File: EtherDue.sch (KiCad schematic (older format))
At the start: 0 parts

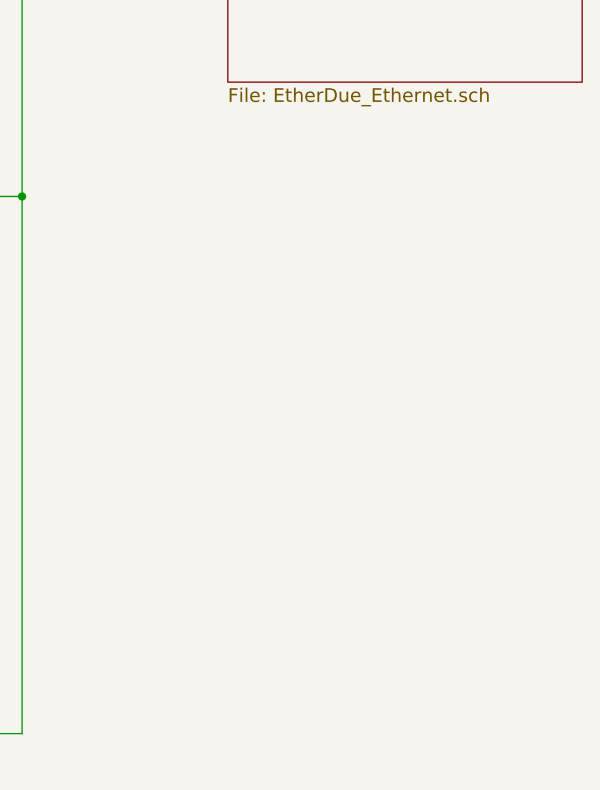
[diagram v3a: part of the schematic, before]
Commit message: Add 24AA025E48 EEPROM w/ unique MAC address
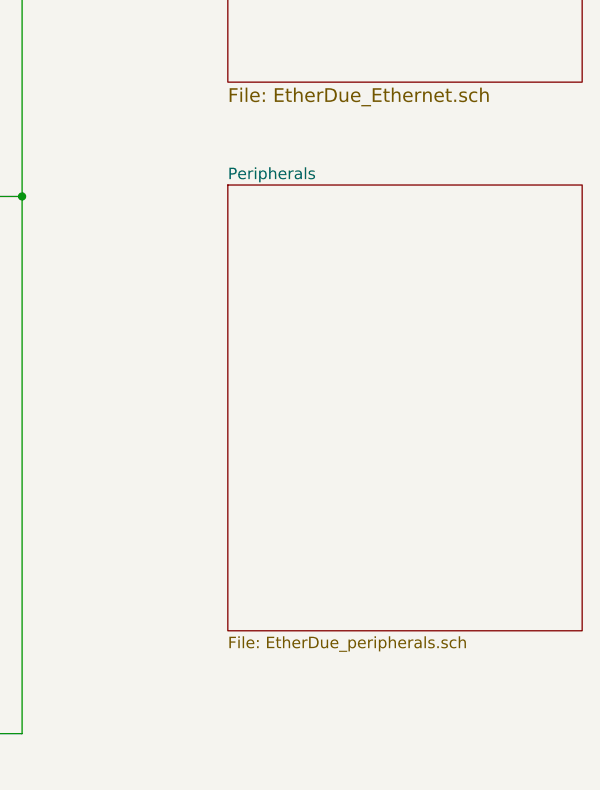
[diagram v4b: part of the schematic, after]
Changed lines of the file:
@@
-EESchema Schematic File Version 2  date Fri 28 Jun 2013 16:34:50 EST
+EESchema Schematic File Version 2  date Thu 04 Jul 2013 10:55:52 EST
 LIBS:freetronics_kicad_sch_lib
 LIBS:power
@@
 $Descr A4 11693 8268
 encoding utf-8
-Sheet 1 6
+Sheet 1 7
 Title ""
-Date "27 jun 2013"
+Date "4 jul 2013"
 Rev ""
 Comp ""
@@
 F2 "/MASTER-RESET" I L 7450 1300 60
 $EndSheet
+$Sheet
+S 7450 3600 1550 1950
+U 51D4D3EB
+F0 "Peripherals" 50
+F1 "EtherDue_peripherals.sch" 50
+$EndSheet
 $EndSCHEMATC

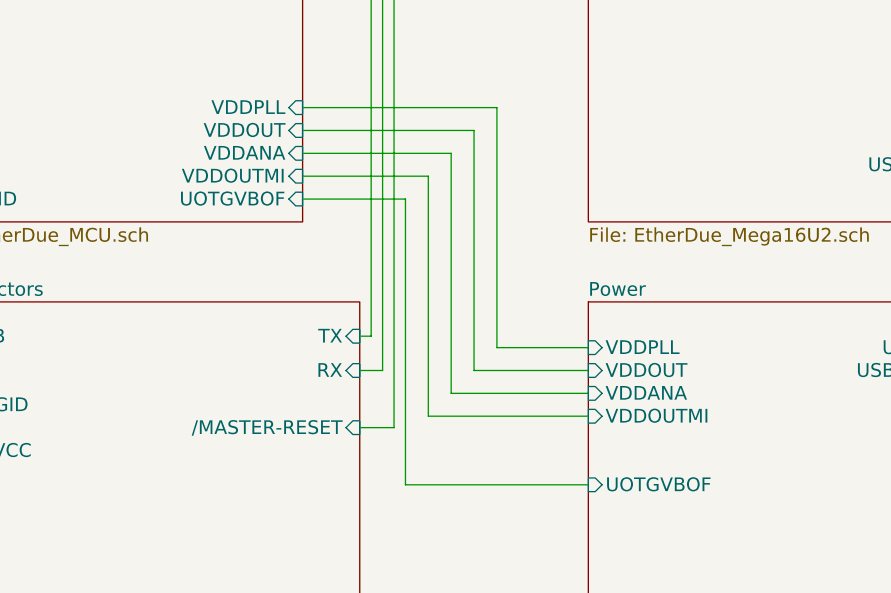
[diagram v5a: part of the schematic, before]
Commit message: Big power fixes: Fix major problem with VDDOUT/1.8V net, rearrange decoupling capacitors
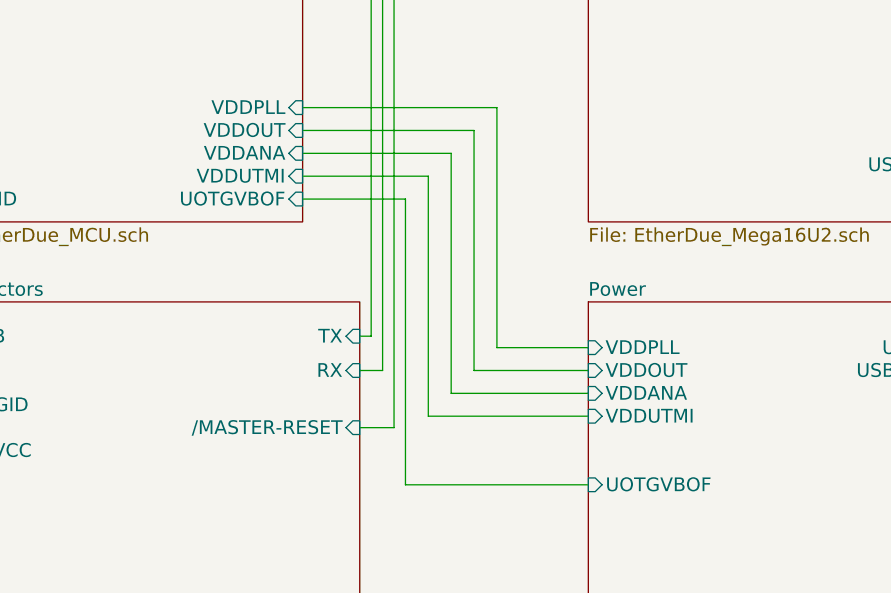
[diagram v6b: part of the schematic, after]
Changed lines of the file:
@@
 F3 "RX" I R 2750 1400 60
 F4 "VDDANA" I R 2750 2800 60
-F5 "VDDOUTMI" I R 2750 2900 60
+F5 "VDDUTMI" I R 2750 2900 60
 F6 "/ERASE_CMD" I R 2750 1850 60
 F7 "VDDPLL" I R 2750 2600 60
@@
 F5 "VDDPLL" I L 4000 3650 60
 F6 "VDDOUT" I L 4000 3750 60
-F7 "VDDOUTMI" I L 4000 3950 60
+F7 "VDDUTMI" I L 4000 3950 60
 F8 "VDDANA" I L 4000 3850 60
 $EndSheet

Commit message: Fix footprint association on resistor network for RJ45 connection
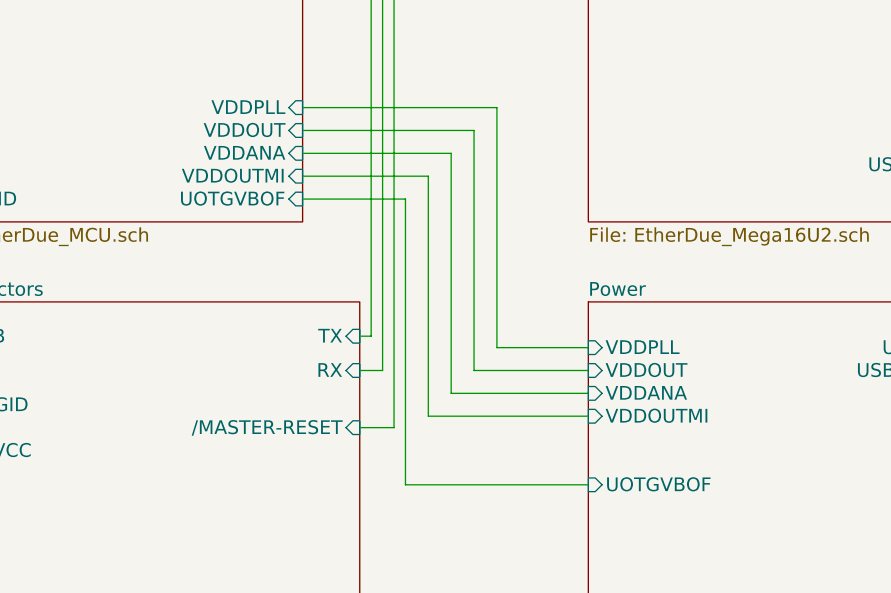
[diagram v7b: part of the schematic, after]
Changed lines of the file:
@@
 LIBS:valves
 LIBS:EtherDue-cache
-EELAYER 24 0
+EELAYER 27 0
 EELAYER END
 $Descr A4 11693 8268
@@
 Sheet 1 7
 Title ""
-Date "4 jul 2013"
+Date "20 nov 2013"
 Rev ""
 Comp ""
@@
 F3 "RX" I R 2750 1400 60
 F4 "VDDANA" I R 2750 2800 60
-F5 "VDDUTMI" I R 2750 2900 60
+F5 "VDDOUTMI" I R 2750 2900 60
 F6 "/ERASE_CMD" I R 2750 1850 60
 F7 "VDDPLL" I R 2750 2600 60
@@
 F5 "VDDPLL" I L 4000 3650 60
 F6 "VDDOUT" I L 4000 3750 60
-F7 "VDDUTMI" I L 4000 3950 60
+F7 "VDDOUTMI" I L 4000 3950 60
 F8 "VDDANA" I L 4000 3850 60
 $EndSheet
